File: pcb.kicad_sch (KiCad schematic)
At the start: 14 parts

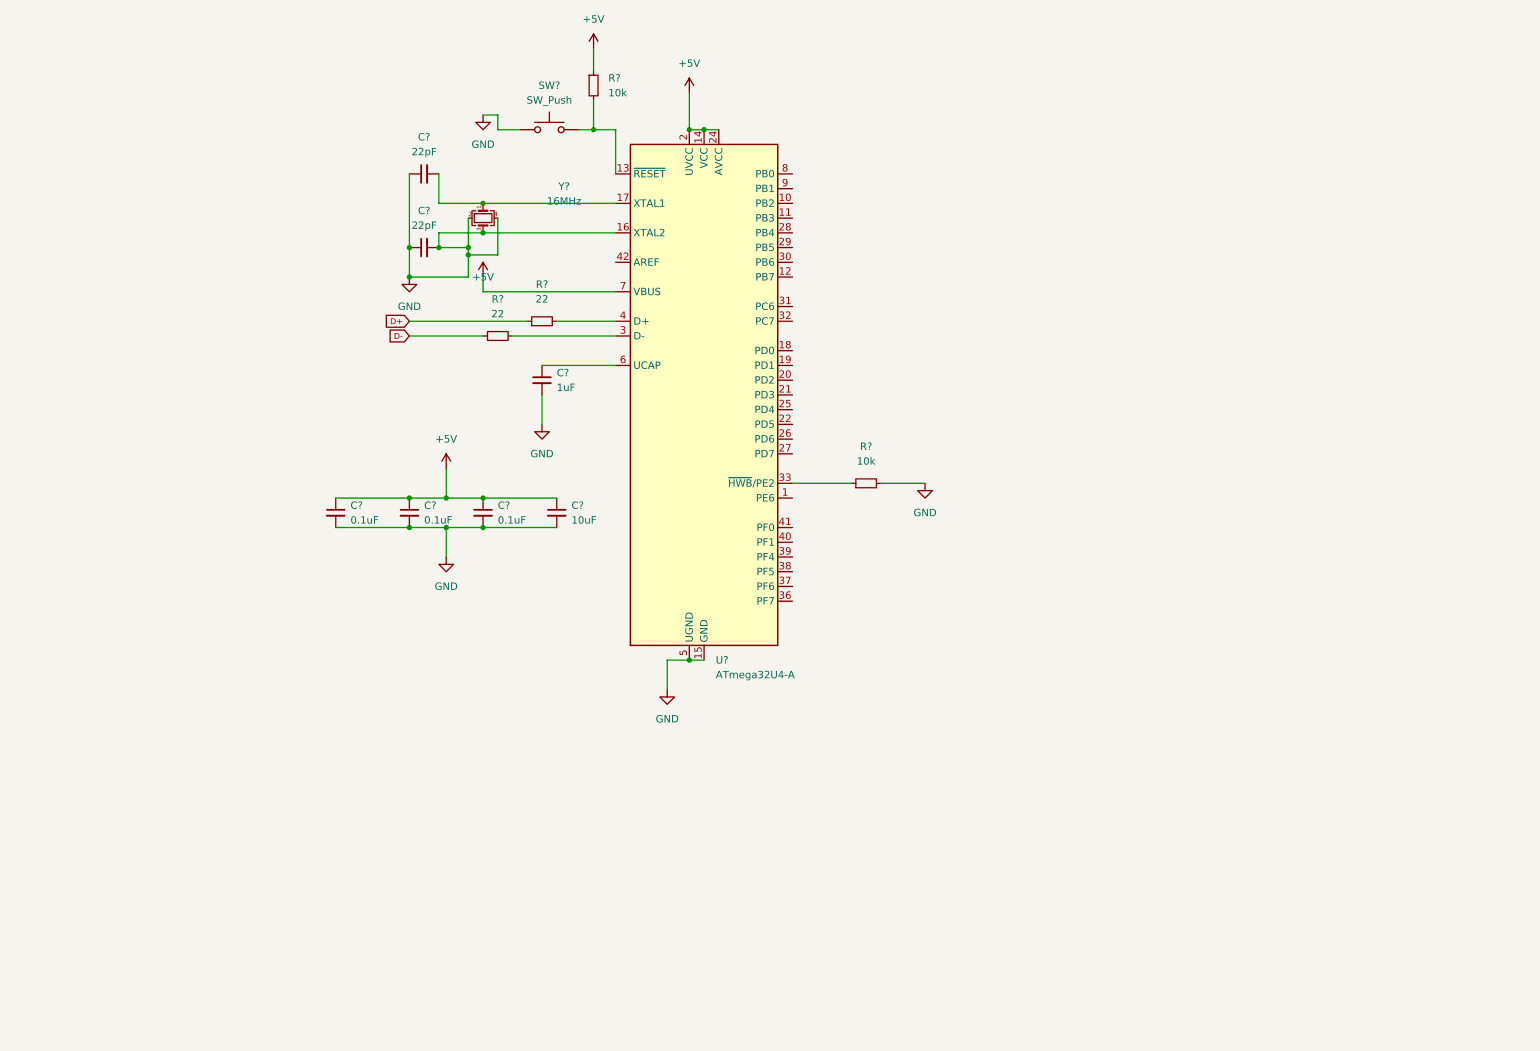
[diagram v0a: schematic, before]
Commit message: added LDC1614 and inductors to schematic
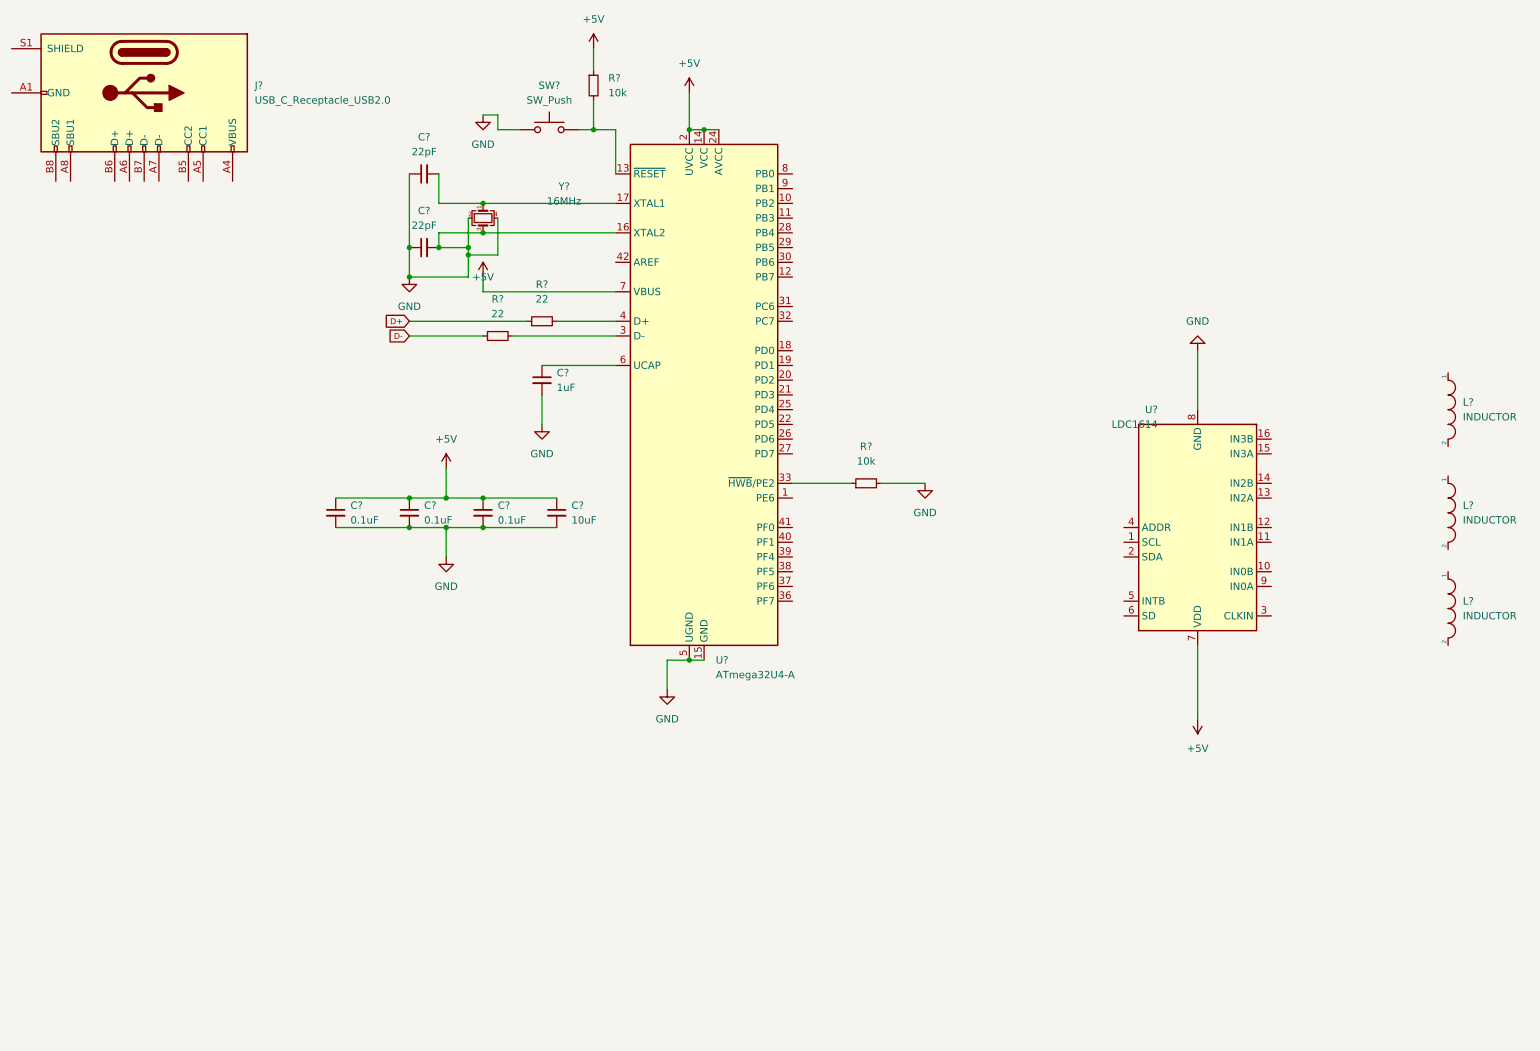
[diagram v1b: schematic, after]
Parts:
- added J?: USB_C_Receptacle_USB2.0, symbol Connector:USB_C_Receptacle_USB2.0
- added L? (x3): INDUCTOR, symbol pspice:INDUCTOR
- added U?: LDC1614, Package_DFN_QFN:WQFN-16-1EP_4x4mm_P0.5mm_EP2.6x2.6mm_ThermalVias, symbol Sensor_Proximity:LDC1614
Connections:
- net +5V: now also U?.7 (VDD)
- net GND: now also U?.17 (GND), U?.8 (GND)
- new net: J?.A1 (GND), J?.A12 (GND), J?.B1 (GND), J?.B12 (GND)
- new net: J?.A4 (VBUS), J?.A9 (VBUS), J?.B4 (VBUS), J?.B9 (VBUS)
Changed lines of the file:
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@@
+    (stroke (width 0) (type default) (color 0 0 0 0))
+  )
+  (wire (pts (xy 224.79 86.36) (xy 224.79 76.2))
     (stroke (width 0) (type default) (color 0 0 0 0))
   )
@@
   )
   (wire (pts (xy 76.2 106.68) (xy 88.9 106.68))
+    (stroke (width 0) (type default) (color 0 0 0 0))
+  )
+  (wire (pts (xy 224.79 139.7) (xy 224.79 127))
     (stroke (width 0) (type default) (color 0 0 0 0))
   )
@@
     (pin "2")
   )
+  (symbol (lib_id "pspice:INDUCTOR") (at 267.97 86.36 270) (unit 1)
+    (in_bom yes) (on_board yes) (fields_autoplaced)
+    (property "Reference" "L?" (id 0) (at 270.51 85.0899 90)
+      (effects (font (size 1.27 1.27)) (justify left))
+    )
+    (property "Value" "INDUCTOR" (id 1) (at 270.51 87.6299 90)
+      (effects (font (size 1.27 1.27)) (justify left))
+    )
+    (property "Footprint" "" (id 2) (at 267.97 86.36 0)
+      (effects (font (size 1.27 1.27)) hide)
+    )
+    (property "Datasheet" "~" (id 3) (at 267.97 86.36 0)
+      (effects (font (size 1.27 1.27)) hide)
+    )
+    (pin "1")
+    (pin "2")
+  )
   (symbol (lib_id "power:+5V") (at 101.6 63.5 0) (unit 1)
     (in_bom yes) (on_board yes)
@@
     (pin "1")
   )
+  (symbol (lib_id "pspice:INDUCTOR") (at 267.97 120.65 270) (unit 1)
+    (in_bom yes) (on_board yes) (fields_autoplaced)
+    (property "Reference" "L?" (id 0) (at 270.51 119.3799 90)
+      (effects (font (size 1.27 1.27)) (justify left))
+    )
+    (property "Value" "INDUCTOR" (id 1) (at 270.51 121.9199 90)
+      (effects (font (size 1.27 1.27)) (justify left))
+    )
+    (property "Footprint" "" (id 2) (at 267.97 120.65 0)
+      (effects (font (size 1.27 1.27)) hide)
+    )
+    (property "Datasheet" "~" (id 3) (at 267.97 120.65 0)
+      (effects (font (size 1.27 1.27)) hide)
+    )
+    (pin "1")
+    (pin "2")
+  )
+  (symbol (lib_id "Sensor_Proximity:LDC1614") (at 224.79 106.68 180) (unit 1)
+    (in_bom yes) (on_board yes)
+    (property "Reference" "U?" (id 0) (at 217.9194 86.36 0)
+      (effects (font (size 1.27 1.27)) (justify left))
+    )
+    (property "Value" "LDC1614" (id 1) (at 217.9194 88.9 0)
+      (effects (font (size 1.27 1.27)) (justify left))
+    )
+    (property "Footprint" "Package_DFN_QFN:WQFN-16-1EP_4x4mm_P0.5mm_EP2.6x2.6mm_ThermalVias" (id 2) (at 217.17 106.68 0)
+      (effects (font (size 1.27 1.27)) hide)
+    )
+    (property "Datasheet" "http://www.ti.com/lit/ds/symlink/ldc1612.pdf" (id 3) (at 224.79 109.22 0)
+      (effects (font (size 1.27 1.27)) hide)
+    )
+    (pin "1")
+    (pin "10")
+    (pin "11")
+    (pin "12")
+    (pin "13")
+    (pin "14")
+    (pin "15")
+    (pin "16")
+    (pin "17")
+    (pin "2")
+    (pin "3")
+    (pin "4")
+    (pin "5")
+    (pin "6")
+    (pin "7")
+    (pin "8")
+    (pin "9")
+  )
   (symbol (lib_id "Device:R_Small") (at 104.14 73.66 90) (unit 1)
     (in_bom yes) (on_board yes) (fields_autoplaced)
@@
     (pin "2")
   )
+  (symbol (lib_id "Connector:USB_C_Receptacle_USB2.0") (at 43.18 31.75 270) (unit 1)
+    (in_bom yes) (on_board yes) (fields_autoplaced)
+    (property "Reference" "J?" (id 0) (at 62.23 30.4799 90)
+      (effects (font (size 1.27 1.27)) (justify left))
+    )
+    (property "Value" "USB_C_Receptacle_USB2.0" (id 1) (at 62.23 33.0199 90)
+      (effects (font (size 1.27 1.27)) (justify left))
+    )
+    (property "Footprint" "" (id 2) (at 43.18 35.56 0)
+      (effects (font (size 1.27 1.27)) hide)
+    )
+    (property "Datasheet" "https://www.usb.org/sites/default/files/documents/usb_type-c.zip" (id 3) (at 43.18 35.56 0)
+      (effects (font (size 1.27 1.27)) hide)
+    )
+    (pin "A1")
+    (pin "A12")
+    (pin "A4")
+    (pin "A5")
+    (pin "A6")
+    (pin "A7")
+    (pin "A8")
+    (pin "A9")
+    (pin "B1")
+    (pin "B12")
+    (pin "B4")
+    (pin "B5")
+    (pin "B6")
+    (pin "B7")
+    (pin "B8")
+    (pin "B9")
+    (pin "S1")
+  )
   (symbol (lib_id "Device:C_Small") (at 91.44 58.42 90) (unit 1)
     (in_bom yes) (on_board yes) (fields_autoplaced)
@@
     (pin "3")
     (pin "4")
+  )
+  (symbol (lib_id "pspice:INDUCTOR") (at 267.97 104.14 270) (unit 1)
+    (in_bom yes) (on_board yes) (fields_autoplaced)
+    (property "Reference" "L?" (id 0) (at 270.51 102.8699 90)
+      (effects (font (size 1.27 1.27)) (justify left))
+    )
+    (property "Value" "INDUCTOR" (id 1) (at 270.51 105.4099 90)
+      (effects (font (size 1.27 1.27)) (justify left))
+    )
+    (property "Footprint" "" (id 2) (at 267.97 104.14 0)
+      (effects (font (size 1.27 1.27)) hide)
+    )
+    (property "Datasheet" "~" (id 3) (at 267.97 104.14 0)
+      (effects (font (size 1.27 1.27)) hide)
+    )
+    (pin "1")
+    (pin "2")
   )
   (symbol (lib_id "Device:R_Small") (at 120.65 30.48 0) (unit 1)
@@
     (pin "9")
   )
+  (symbol (lib_id "power:+5V") (at 224.79 139.7 180) (unit 1)
+    (in_bom yes) (on_board yes) (fields_autoplaced)
+    (property "Reference" "#PWR?" (id 0) (at 224.79 135.89 0)
+      (effects (font (size 1.27 1.27)) hide)
+    )
+    (property "Value" "+5V" (id 1) (at 224.79 144.78 0))
+    (property "Footprint" "" (id 2) (at 224.79 139.7 0)
+      (effects (font (size 1.27 1.27)) hide)
+    )
+    (property "Datasheet" "" (id 3) (at 224.79 139.7 0)
+      (effects (font (size 1.27 1.27)) hide)
+    )
+    (pin "1")
+  )
   (symbol (lib_id "power:GND") (at 95.25 111.76 0) (unit 1)
     (in_bom yes) (on_board yes) (fields_autoplaced)
@@
     (pin "2")
   )
+  (symbol (lib_id "power:GND") (at 224.79 76.2 180) (unit 1)
+    (in_bom yes) (on_board yes) (fields_autoplaced)
+    (property "Reference" "#PWR?" (id 0) (at 224.79 69.85 0)
+      (effects (font (size 1.27 1.27)) hide)
+    )
+    (property "Value" "GND" (id 1) (at 224.79 71.12 0))
+    (property "Footprint" "" (id 2) (at 224.79 76.2 0)
+      (effects (font (size 1.27 1.27)) hide)
+    )
+    (property "Datasheet" "" (id 3) (at 224.79 76.2 0)
+      (effects (font (size 1.27 1.27)) hide)
+    )
+    (pin "1")
+  )
   (sheet_instances
     (path "/" (page "1"))
@@
       (reference "#PWR?") (unit 1) (value "GND") (footprint "")
     )
+    (path "/d1e27647-99a1-463b-aea2-38534a70b477"
+      (reference "#PWR?") (unit 1) (value "+5V") (footprint "")
+    )
     (path "/daf1acdc-489c-44c7-8619-5d78e71eaa1b"
       (reference "#PWR?") (unit 1) (value "GND") (footprint "")
@@
       (reference "#PWR?") (unit 1) (value "+5V") (footprint "")
     )
+    (path "/f149ba39-04f4-4b80-942c-f4b50c1c2c60"
+      (reference "#PWR?") (unit 1) (value "GND") (footprint "")
+    )
     (path "/0fe8aca2-6fe3-4053-b678-c0518ab3b34f"
       (reference "C?") (unit 1) (value "0.1uF") (footprint "")
@@
       (reference "C?") (unit 1) (value "0.1uF") (footprint "")
     )
+    (path "/42aa49ba-1ab2-400e-b54b-dcba2e8455ee"
+      (reference "J?") (unit 1) (value "USB_C_Receptacle_USB2.0") (footprint "")
+    )
+    (path "/33daa439-9752-4789-8e95-b8b2e4b2f5d8"
+      (reference "L?") (unit 1) (value "INDUCTOR") (footprint "")
+    )
+    (path "/380de79c-ffac-490a-b5b2-bcb65a4d03ef"
+      (reference "L?") (unit 1) (value "INDUCTOR") (footprint "")
+    )
+    (path "/74ab0038-0bde-4f92-b2c9-fe602d5bbb2f"
+      (reference "L?") (unit 1) (value "INDUCTOR") (footprint "")
+    )
     (path "/210238e3-f679-475e-bfa8-25f295955ad0"
       (reference "R?") (unit 1) (value "22") (footprint "")
@@
       (reference "SW?") (unit 1) (value "SW_Push") (footprint "")
     )
+    (path "/3d558eda-44a3-435d-bd94-2d16394cb460"
+      (reference "U?") (unit 1) (value "LDC1614") (footprint "Package_DFN_QFN:WQFN-16-1EP_4x4mm_P0.5mm_EP2.6x2.6mm_ThermalVias")
+    )
     (path "/ce66623f-078d-49d7-b158-6c77df686640"
